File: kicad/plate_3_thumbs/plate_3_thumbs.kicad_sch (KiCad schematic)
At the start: 70 parts, among them SW1 EC_SW

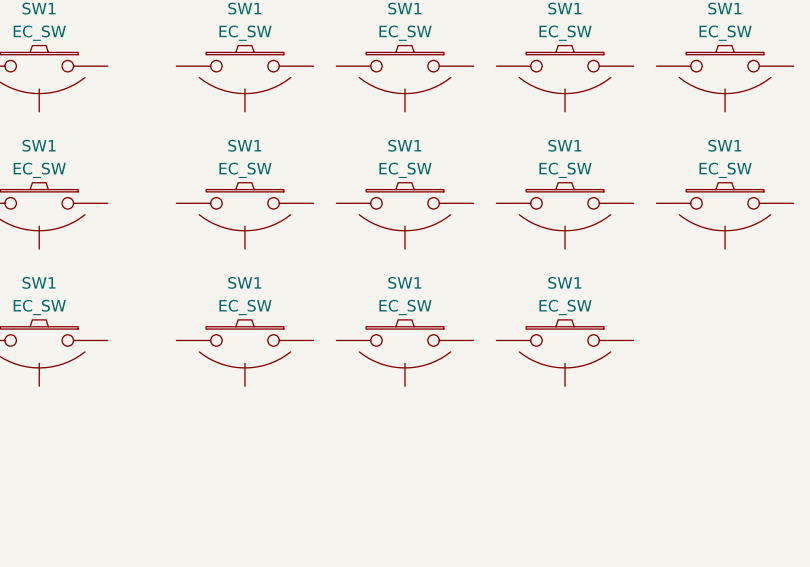
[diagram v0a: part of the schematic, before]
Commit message: fix 3-thumb plate kibot issue
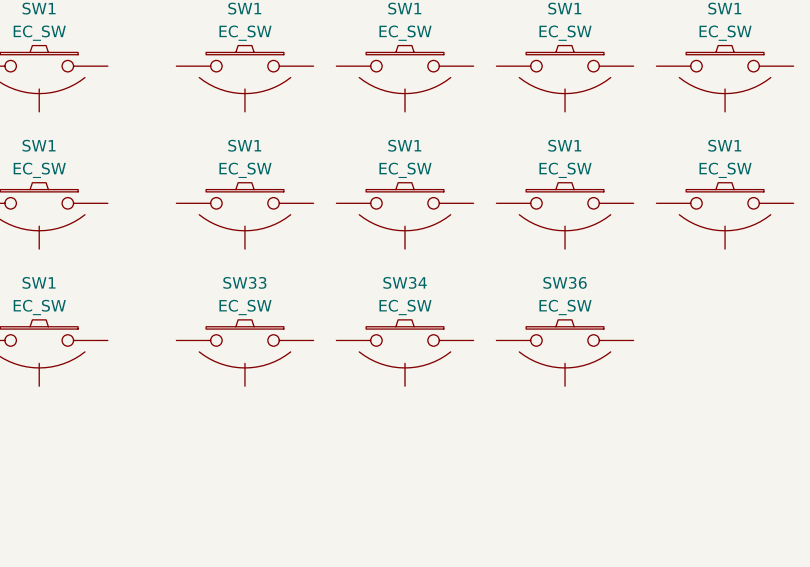
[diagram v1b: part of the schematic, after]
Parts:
- removed SW1 (x3): EC_SW, capacitive_sensors:plate_cut_1U_topre, symbol cipulot_parts:EC_SW
- added SW33, SW34, SW36: EC_SW, capacitive_sensors:plate_cut_1U_topre, symbol cipulot_parts:EC_SW
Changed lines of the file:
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@@
   (symbol (lib_id "cipulot_parts:EC_SW") (at 119.38 78.74 0) (mirror y) (unit 1)
     (in_bom no) (on_board yes) (dnp no)
-    (property "Reference" "SW1" (at 119.38 72.39 0)
+    (property "Reference" "SW33" (at 119.38 72.39 0)
       (effects (font (size 1.27 1.27)))
     )
@@
     (pin "3")
     (instances
-      (project "tako"
-        (path "/7b28ce14-5c63-4c9f-9bca-abf529f54075"
-          (reference "SW1") (unit 1)
-        )
-      )
-      (project "tako"
-        (path "/9d8265e2-df3b-4900-a886-1f487fd3d916"
-          (reference "SW1") (unit 1)
-        )
-      )
       (project "plate_3_thumbs"
         (path "/ca0d59d2-7f9b-4344-99bc-39bc2c8c88cb"
@@
     )
   )
+  (symbol (lib_id "cipulot_parts:EC_SW") (at 154.94 78.74 0) (mirror y) (unit 1)
+    (in_bom no) (on_board yes) (dnp no)
+    (property "Reference" "SW36" (at 154.94 72.39 0)
+      (effects (font (size 1.27 1.27)))
+    )
+    (property "Value" "EC_SW" (at 154.94 74.93 0)
+      (effects (font (size 1.27 1.27)))
+    )
+    (property "Footprint" "capacitive_sensors:plate_cut_1U_topre" (at 154.94 78.74 0)
+      (effects (font (size 1.27 1.27)) hide)
+    )
+    (property "Datasheet" "" (at 154.94 78.74 0)
+      (effects (font (size 1.27 1.27)))
+    )
+    (pin "1")
+    (pin "2")
+    (pin "3")
+    (instances
+      (project "plate_3_thumbs"
+        (path "/ca0d59d2-7f9b-4344-99bc-39bc2c8c88cb"
+          (reference "SW36") (unit 1)
+        )
+      )
+    )
+  )
   (symbol (lib_id "cipulot_parts:EC_SW") (at 119.38 63.5 0) (mirror y) (unit 1)
     (in_bom no) (on_board yes) (dnp no)
@@
     )
   )
-  (symbol (lib_id "cipulot_parts:EC_SW") (at 137.16 78.74 0) (mirror y) (unit 1)
-    (in_bom no) (on_board yes) (dnp no)
-    (property "Reference" "SW1" (at 137.16 72.39 0)
-      (effects (font (size 1.27 1.27)))
-    )
-    (property "Value" "EC_SW" (at 137.16 74.93 0)
-      (effects (font (size 1.27 1.27)))
-    )
-    (property "Footprint" "capacitive_sensors:plate_cut_1U_topre" (at 137.16 78.74 0)
-      (effects (font (size 1.27 1.27)) hide)
-    )
-    (property "Datasheet" "" (at 137.16 78.74 0)
-      (effects (font (size 1.27 1.27)))
-    )
-    (pin "1")
-    (pin "2")
-    (pin "3")
-    (instances
-      (project "tako"
-        (path "/7b28ce14-5c63-4c9f-9bca-abf529f54075"
-          (reference "SW1") (unit 1)
-        )
-      )
-      (project "tako"
-        (path "/9d8265e2-df3b-4900-a886-1f487fd3d916"
-          (reference "SW1") (unit 1)
-        )
-      )
-      (project "plate_3_thumbs"
-        (path "/ca0d59d2-7f9b-4344-99bc-39bc2c8c88cb"
-          (reference "SW34") (unit 1)
-        )
-      )
-    )
-  )
   (symbol (lib_id "cipulot_parts:EC_SW") (at 137.16 48.26 0) (mirror y) (unit 1)
     (in_bom no) (on_board yes) (dnp no)
@@
         (path "/ca0d59d2-7f9b-4344-99bc-39bc2c8c88cb"
           (reference "SW4") (unit 1)
-        )
-      )
-    )
-  )
-  (symbol (lib_id "cipulot_parts:EC_SW") (at 154.94 78.74 0) (mirror y) (unit 1)
-    (in_bom no) (on_board yes) (dnp no)
-    (property "Reference" "SW1" (at 154.94 72.39 0)
-      (effects (font (size 1.27 1.27)))
-    )
-    (property "Value" "EC_SW" (at 154.94 74.93 0)
-      (effects (font (size 1.27 1.27)))
-    )
-    (property "Footprint" "capacitive_sensors:plate_cut_1U_topre" (at 154.94 78.74 0)
-      (effects (font (size 1.27 1.27)) hide)
-    )
-    (property "Datasheet" "" (at 154.94 78.74 0)
-      (effects (font (size 1.27 1.27)))
-    )
-    (pin "1")
-    (pin "2")
-    (pin "3")
-    (instances
-      (project "tako"
-        (path "/7b28ce14-5c63-4c9f-9bca-abf529f54075"
-          (reference "SW1") (unit 1)
-        )
-      )
-      (project "tako"
-        (path "/9d8265e2-df3b-4900-a886-1f487fd3d916"
-          (reference "SW1") (unit 1)
-        )
-      )
-      (project "plate_3_thumbs"
-        (path "/ca0d59d2-7f9b-4344-99bc-39bc2c8c88cb"
-          (reference "SW36") (unit 1)
         )
       )
@@
         )
       )
+    )
+  )
+  (symbol (lib_id "cipulot_parts:EC_SW") (at 137.16 78.74 0) (mirror y) (unit 1)
+    (in_bom no) (on_board yes) (dnp no)
+    (property "Reference" "SW34" (at 137.16 72.39 0)
+      (effects (font (size 1.27 1.27)))
+    )
+    (property "Value" "EC_SW" (at 137.16 74.93 0)
+      (effects (font (size 1.27 1.27)))
+    )
+    (property "Footprint" "capacitive_sensors:plate_cut_1U_topre" (at 137.16 78.74 0)
+      (effects (font (size 1.27 1.27)) hide)
+    )
+    (property "Datasheet" "" (at 137.16 78.74 0)
+      (effects (font (size 1.27 1.27)))
+    )
+    (pin "1")
+    (pin "2")
+    (pin "3")
+    (instances
+      (project "plate_3_thumbs"
+        (path "/ca0d59d2-7f9b-4344-99bc-39bc2c8c88cb"
+          (reference "SW34") (unit 1)
+        )
+      )
